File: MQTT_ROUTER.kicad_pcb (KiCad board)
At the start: 2 copper layers, 100 x 100 mm, 84 parts, among them J1 Conn_2Rows-07Pins, J2 Conn_02x07_Odd_Even, J3 Screw_Terminal_01x02, J4 Screw_Terminal_01x03, J5 Screw_Terminal_01x03, J6 Screw_Terminal_01x04, J7 Screw_Terminal_01x06, K1 SANYOU_SRD_Form_C, K2 SANYOU_SRD_Form_C, Q1 SS8050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

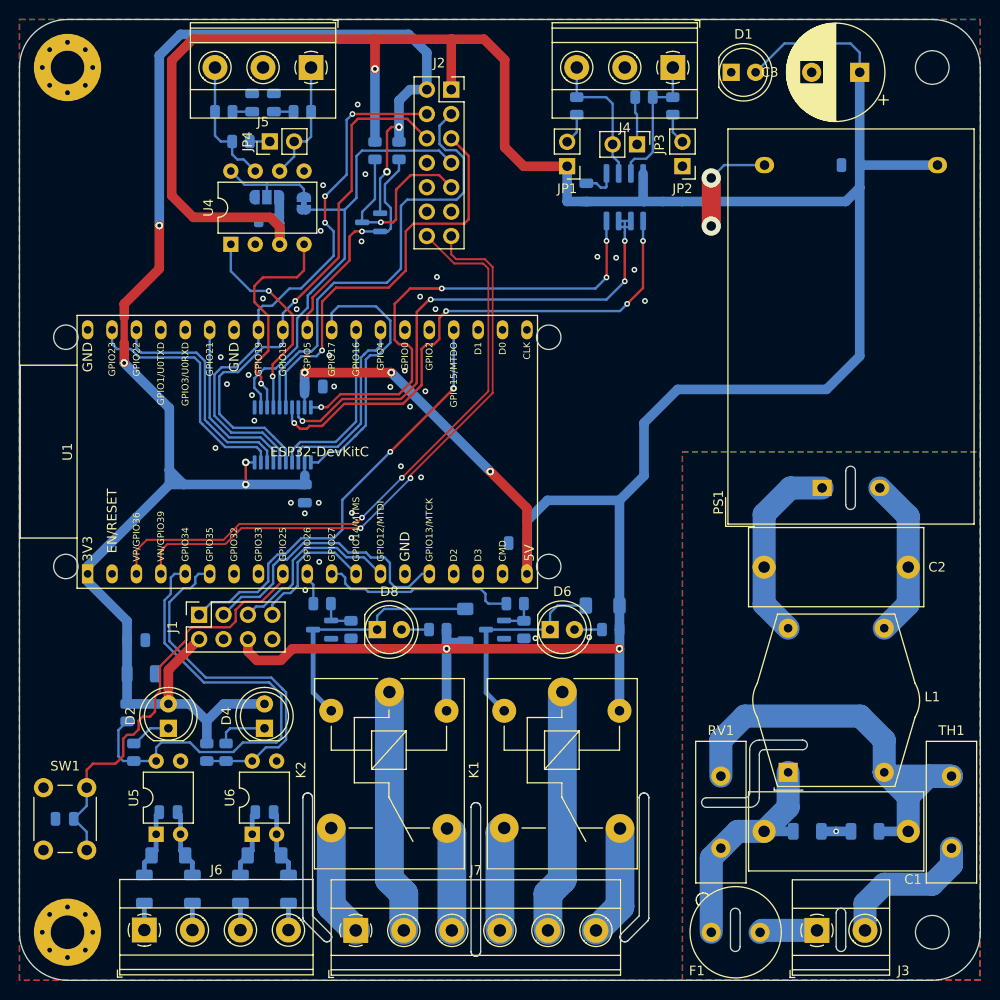
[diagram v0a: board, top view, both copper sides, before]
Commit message: Reparar ubicación de serigrafías y errores de DRC. Mejorar pistas de 5V y 3V.
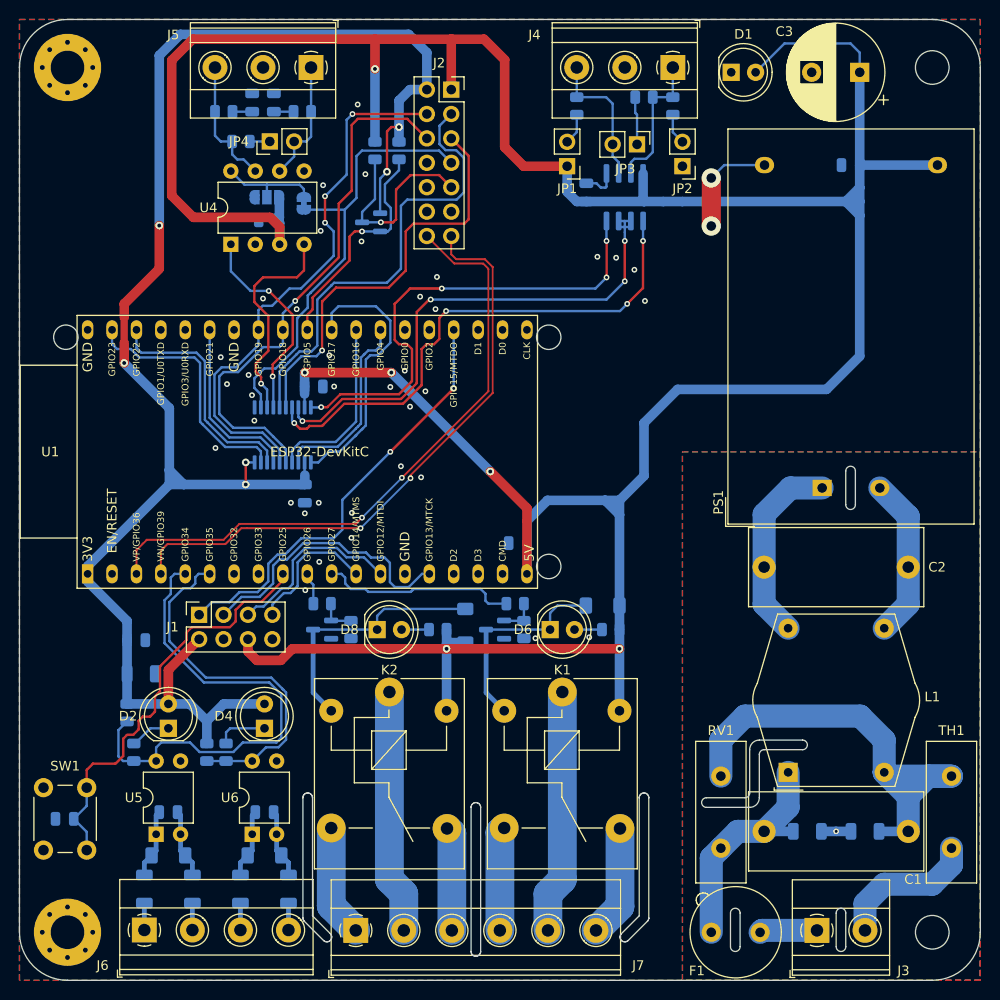
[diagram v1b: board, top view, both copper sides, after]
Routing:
- net +5V: track 347.3 -> 352.4 mm
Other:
- outline, holes or cut-outs redrawn

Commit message: Actualizar componentes, pistas e imágenes
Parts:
- U1: value ESP32-DevKitC -> ESP32-DevKit-USB-C; footprint PCM_Espressif:ESP32-DevKitC -> ESP32:ESP32-DevKit-USB-C
- moved C6 10.2 mm to (140.2, 109.5)
- moved C9 2.52 mm to (125.7, 104.3)
- moved C10 2.50 mm to (126.6, 93.2)
- moved U2 2.50 mm to (123.4, 98.2)
- moved C4 1.50 mm to (183.5, 70.2)
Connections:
- U1 pad 1: +3V3 -> unconnected-(U1-CHIP_PU-Pad1)
- U1 pad 10: /K2 -> /K1
- U1 pad 11: /K1 -> /MTMS
- U1 pad 12: /MTMS -> /MTDI
- U1 pad 13: /MTDI -> /MTCK
- U1 pad 15: /MTCK -> +5V
- U1 pad 16: unconnected-(U1-SD_DATA2/GPIO9-Pad16) -> +3V3
- U1 pad 17: unconnected-(U1-SD_DATA3/GPIO10-Pad17) -> GND
- U1 pad 18: unconnected-(U1-CMD-Pad18) -> /MTDO
- U1 pad 19: +5V -> unconnected-(U1-ADC2_CH2/GPIO2-Pad19)
- U1 pad 2: unconnected-(U1-CHIP_PU-Pad2) -> /S_VP
- U1 pad 20: unconnected-(U1-SD_CLK/GPIO6-Pad20) -> /DERE_LO
- U1 pad 21: unconnected-(U1-SD_DATA0/GPIO7-Pad21) -> /RO_LO
- U1 pad 22: unconnected-(U1-SD_DATA1/GPIO8-Pad22) -> /DI_LO
- U1 pad 23: /MTDO -> /SS_LO
- U1 pad 24: unconnected-(U1-ADC2_CH2/GPIO2-Pad24) -> /SDA_LO
- U1 pad 25: unconnected-(U1-GPIO0/BOOT/ADC2_CH1-Pad25) -> /SCL_LO
- U1 pad 26: /DERE_LO -> /TXD_LO
- U1 pad 27: /RO_LO -> unconnected-(U1-U0RXD/GPIO3-Pad27)
- U1 pad 28: /DI_LO -> unconnected-(U1-U0TXD/GPIO1-Pad28)
- U1 pad 29: /SS_LO -> /RXD_LO
- U1 pad 3: /S_VP -> /S_VN
- U1 pad 30: /SDA_LO -> /RS_LO
- U1 pad 4: /S_VN -> /OP1
- U1 pad 5: /OP1 -> /OP2
- U1 pad 6: /OP2 -> unconnected-(U1-32K_XP/GPIO32/ADC1_CH4-Pad6)
- U1 pad 8: unconnected-(U1-32K_XN/GPIO33/ADC1_CH5-Pad8) -> /CFG_MODE
- U1 pad 9: /CFG_MODE -> /K2
- U2 pad 1: /DI_LO -> /DERE_LO
- U2 pad 17: /RO_HI -> /DI_HI
- U2 pad 18: /DERE_HI -> /RO_HI
- U2 pad 20: /DI_HI -> /DERE_HI
- U2 pad 3: /DERE_LO -> /RO_LO
- U2 pad 4: /RO_LO -> /DI_LO
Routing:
- net +5V: track 352.4 -> 237.9 mm, vias 6 -> 7
- net +3V3: track 175.4 -> 197.2 mm, vias 6 -> 8
- net /DI_LO: track 28.6 -> 19.6 mm
- net /SS_LO: track 24.2 -> 30.0 mm
- net /RS_HI: track 46.4 -> 51.7 mm
- net /DERE_HI: track 55.5 -> 50.6 mm
- net /MTCK: track 29.2 -> 25.0 mm
- net /CFG_MODE: track 43.9 -> 48.0 mm
- net /K1: track 20.5 -> 24.2 mm, vias 0 -> 1
- net /SCL_HI: track 47.6 -> 51.0 mm
- net /MTMS: track 14.4 -> 17.6 mm
- net /SDA_HI: track 43.9 -> 47.0 mm
- net /DERE_LO: track 20.0 -> 16.8 mm
- net /S_VP: track 66.5 -> 63.5 mm
- net /TXD_HI: track 21.7 -> 24.3 mm, vias 2 -> 1
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- added copper zone on B.Cu, net +5V
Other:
- outline, holes or cut-outs redrawn

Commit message: Actualizar PCB
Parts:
- removed F1: 0.5A, Fuse:Fuseholder_TR5_Littelfuse_No560_No460
- removed PS1: HLK-5M05, Converter_ACDC:Converter_ACDC_Hi-Link_HLK-5Mxx
- removed RV1: 14D271K, Capacitor_THT:C_Disc_D14.5mm_W5.0mm_P7.50mm
- added C17: 470uF 16V, Capacitor_THT:CP_Radial_D10.0mm_P5.00mm, F.Cu at (154.2, 79.0)
- added D10: SS36, Diode_SMD:D_SMC, F.Cu at (177.7, 115.2)
- added D11: SS36, Diode_SMD:D_SMC, F.Cu at (168.4, 104.2)
- added D12: 1N47xxA, Diode_THT:D_DO-41_SOD81_P10.16mm_Horizontal, F.Cu at (167.3, 142.4)
- added Q4: IRLZ44N, Package_TO_SOT_THT:TO-220-3_Horizontal_TabDown, F.Cu at (169.5, 139.5)
- added U7: LM2596S-5, Package_TO_SOT_SMD:TO-263-5_TabPin3, F.Cu at (177.7, 101.4)
- C1: value 0.47uF X2 -> 100uF 50V; footprint Capacitor_THT:C_Rect_L18.0mm_W8.0mm_P15.00mm_FKS3_FKP3 -> Capacitor_THT:CP_Radial_D10.0mm_P5.00mm
- C2: value 0.47uF X2 -> 100n; footprint Capacitor_THT:C_Rect_L18.0mm_W8.0mm_P15.00mm_FKS3_FKP3 -> Capacitor_SMD:C_0805_2012Metric; moved to B.Cu
- H1, H2: value MountingHole -> MountingHole_Pad; footprint MountingHole:MountingHole_3.5mm -> MountingHole:MountingHole_3.5mm_Pad_Via
- L1: value L_Coupled -> 47uH; footprint Inductor_THT:Choke_Schaffner_RN112-04-17.7x17.1mm -> Inductor_SMD:L_Bourns_SRR1260
- R1: value 510k -> 100; footprint Resistor_SMD:R_1206_3216Metric -> Resistor_SMD:R_0805_2012Metric
- R2: value 510k -> 20k; footprint Resistor_SMD:R_1206_3216Metric -> Resistor_SMD:R_0805_2012Metric
- TH1: value 8D-10 -> XF250; footprint Capacitor_THT:C_Disc_D14.5mm_W5.0mm_P7.50mm -> Fuse:Fuse_BelFuse_0ZRE0125FF_L21.2mm_W5.3mm
- moved L1 46.1 mm to (176.4, 87.3), turned to 180 degrees
- moved C2 30.6 mm to (172.9, 142.4)
- moved C4 30.4 mm to (170.6, 97.7), turned to -90 degrees
- moved C1 24.1 mm to (167.3, 117.0), turned to 90 degrees
- moved C3 20.3 mm to (171.8, 75.1), turned to 0 degrees
- moved TH1 17.4 mm to (179.4, 134.7)
- moved H1 15.0 mm to (178.5, 150.0)
- moved H2 15.0 mm to (178.5, 60.0)
- moved J3 14.8 mm to (166.7, 149.8)
- moved R2 13.3 mm to (173.6, 136.3)
- moved R3 11.1 mm to (175.7, 67.2), turned to 180 degrees
- moved R1 10.9 mm to (170.1, 136.3)
- moved D1 10.9 mm to (181.2, 67.2), turned to 180 degrees
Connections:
- net /FUENTE/N renamed Net-(J3-Pin_2)
- net Earth renamed Net-(D12-A)
- C1 pad 1: Net-(C1-Pad1) -> /FUENTE/LPROT
- C1 pad 2: Net-(C1-Pad2) -> GND
- C2 pad 1: Net-(PS1-AC/L) -> /FUENTE/LPROT
- C2 pad 2: Net-(PS1-AC/N) -> GND
- J3 pad 1: /FUENTE/L -> GND
- L1 pad 1: Net-(C1-Pad1) -> Net-(D11-K)
- L1 pad 2: Net-(PS1-AC/L) -> +5V
- R1 pad 2: Net-(C1-Pad1) -> Net-(Q4-G)
- R2 pad 2: Net-(C1-Pad2) -> GND
- TH1 pad 2: Net-(C1-Pad2) -> Net-(D10-A)
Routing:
- net Net-(C1-Pad2): track 48.9 -> 0.00 mm
- net /FUENTE/LPROT: track 0.00 -> 47.8 mm
- net Net-(D11-K): track 0.00 -> 37.0 mm
- net +5V: track 237.9 -> 269.2 mm, vias 7 -> 14
- net Net-(C1-Pad1): track 24.6 -> 0.00 mm
- net Net-(PS1-AC/L): track 20.1 -> 0.00 mm
- net Net-(PS1-AC/N): track 16.9 -> 0.00 mm
- net GND: track 14.8 -> 3.70 mm, vias 68 -> 71
- net Net-(D12-A): track 3.07 -> 12.7 mm
- net Net-(D10-A): track 0.00 -> 9.32 mm
- net Net-(J3-Pin_2): track 15.2 -> 21.9 mm
- net /FUENTE/L: track 6.00 -> 0.00 mm
- net Net-(D1-A): track 6.22 -> 2.05 mm
- net Net-(Q4-G): track 0.00 -> 3.31 mm
- removed copper zone on B.Cu, net Net-(D12-A)
- removed copper zone on F.Cu, net Net-(D12-A)
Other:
- board size 100 x 100 mm -> 85 x 100 mm

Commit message: Actualizar zener a 1N4752A (33V)
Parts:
- D12: value 1N47xxA -> 1N4752A
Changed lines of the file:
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@@
 		(tags "LED")
 		(property "Reference" "D1"
-			(at 1.27 -3.96 360)
+			(at 1.27 -3.96 0)
 			(layer "F.SilkS")
 			(effects
@@
 		)
 		(property "Value" "LED_RED"
-			(at 1.27 3.96 360)
+			(at 1.27 3.96 0)
 			(layer "F.Fab")
 			(effects
@@
 		)
 		(property "Footprint" "LED_THT:LED_D5.0mm"
-			(at 0 0 360)
+			(at 0 0 0)
 			(layer "F.Fab")
 			(hide yes)
@@
 		)
 		(property "Datasheet" ""
-			(at 0 0 360)
+			(at 0 0 0)
 			(layer "F.Fab")
 			(hide yes)
@@
 		)
 		(property "Description" "Light emitting diode"
-			(at 0 0 360)
+			(at 0 0 0)
 			(layer "F.Fab")
 			(hide yes)
@@
 		)
 		(fp_text user "${REFERENCE}"
-			(at 1.27 0 360)
+			(at 1.27 0 0)
 			(layer "F.Fab")
 			(effects
@@
 			)
 		)
-		(property "Value" "1N47xxA"
+		(property "Value" "1N4752A"
 			(at 5.08 2.47 0)
 			(layer "F.Fab")
@@
 		(tags "resistor")
 		(property "Reference" "R3"
-			(at 0 1.7 360)
+			(at 0 1.7 0)
 			(layer "B.SilkS")
 			(effects
@@
 		)
 		(property "Value" "330"
-			(at 0 -1.65 360)
+			(at 0 -1.65 0)
 			(layer "B.Fab")
 			(effects
@@
 		)
 		(fp_text user "${REFERENCE}"
-			(at 0 0 360)
+			(at 0 0 0)
 			(layer "B.Fab")
 			(effects

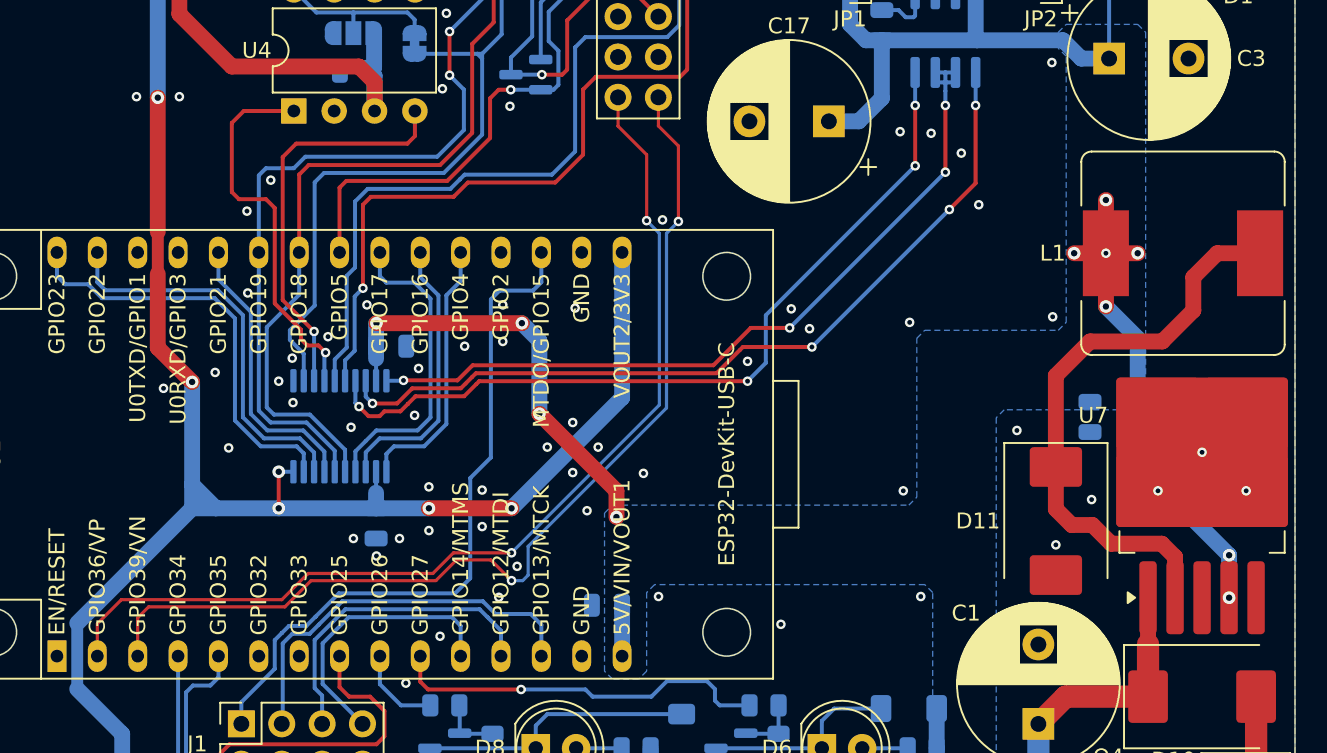
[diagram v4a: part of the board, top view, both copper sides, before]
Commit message: Ajustar grosor de pistas S_VP/S_VN
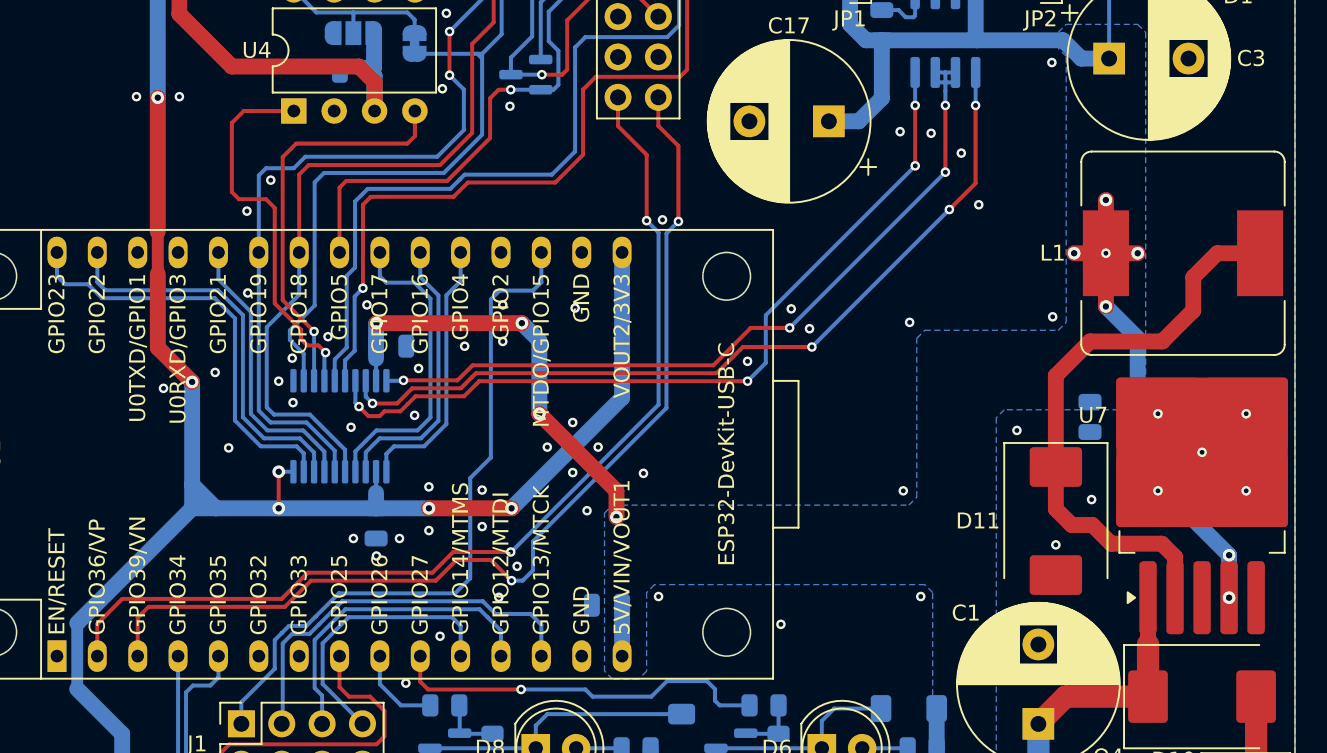
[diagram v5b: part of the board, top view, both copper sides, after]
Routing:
- net GND: vias 71 -> 73
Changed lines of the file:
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@@
+	)
+	(via
+		(at 180.425 97.45)
+		(size 0.6)
+		(drill 0.3)
+		(layers "F.Cu" "B.Cu")
+		(free yes)
+		(net 1)
 	)
 	(via
@@
 	(via
 		(at 151.15 110.7)
+		(size 0.6)
+		(drill 0.3)
+		(layers "F.Cu" "B.Cu")
+		(free yes)
+		(net 1)
+	)
+	(via
+		(at 174.875 97.45)
 		(size 0.6)
 		(drill 0.3)
@@
 	)
 	(segment
+		(start 119.936396 109.6)
+		(end 121.586396 107.95)
+		(width 0.25)
+		(layer "F.Cu")
+		(net 6)
+	)
+	(segment
 		(start 129.436396 107.95)
-		(end 121.586396 107.95)
-		(width 0.2)
-		(layer "F.Cu")
-		(net 6)
-	)
-	(segment
-		(start 119.936396 109.6)
+		(end 130.736396 106.65)
+		(width 0.25)
+		(layer "F.Cu")
+		(net 6)
+	)
+	(segment
+		(start 110.67656 112.7)
+		(end 110.67656 110.28344)
+		(width 0.25)
+		(layer "F.Cu")
+		(net 6)
+	)
+	(segment
+		(start 132.9 106.65)
+		(end 134.2 107.95)
+		(width 0.25)
+		(layer "F.Cu")
+		(net 6)
+	)
+	(segment
+		(start 143.44 79.34)
+		(end 143.44 77.54)
+		(width 0.25)
+		(layer "F.Cu")
+		(net 6)
+	)
+	(segment
+		(start 121.586396 107.95)
+		(end 129.436396 107.95)
+		(width 0.25)
+		(layer "F.Cu")
+		(net 6)
+	)
+	(segment
+		(start 130.736396 106.65)
+		(end 132.9 106.65)
+		(width 0.25)
+		(layer "F.Cu")
+		(net 6)
+	)
+	(segment
+		(start 110.67656 110.28344)
 		(end 111.36 109.6)
-		(width 0.2)
-		(layer "F.Cu")
-		(net 6)
-	)
-	(segment
-		(start 121.586396 107.95)
+		(width 0.25)
+		(layer "F.Cu")
+		(net 6)
+	)
+	(segment
+		(start 144.7 80.6)
+		(end 143.44 79.34)
+		(width 0.25)
+		(layer "F.Cu")
+		(net 6)
+	)
+	(segment
+		(start 111.36 109.6)
 		(end 119.936396 109.6)
-		(width 0.2)
-		(layer "F.Cu")
-		(net 6)
-	)
-	(segment
-		(start 132.9 106.65)
-		(end 130.736396 106.65)
-		(width 0.2)
-		(layer "F.Cu")
-		(net 6)
-	)
-	(segment
-		(start 143.44 77.54)
-		(end 143.44 79.34)
-		(width 0.2)
-		(layer "F.Cu")
-		(net 6)
-	)
-	(segment
-		(start 130.736396 106.65)
-		(end 129.436396 107.95)
-		(width 0.2)
-		(layer "F.Cu")
-		(net 6)
-	)
-	(segment
-		(start 111.36 109.6)
-		(end 110.67656 110.28344)
-		(width 0.2)
-		(layer "F.Cu")
-		(net 6)
-	)
-	(segment
-		(start 134.2 107.95)
-		(end 132.9 106.65)
-		(width 0.2)
-		(layer "F.Cu")
-		(net 6)
-	)
-	(segment
-		(start 144.7 80.6)
-		(end 144.7 85.35)
-		(width 0.2)
-		(layer "F.Cu")
-		(net 6)
-	)
-	(segment
-		(start 110.67656 110.28344)
-		(end 110.67656 112.7)
-		(width 0.2)
-		(layer "F.Cu")
-		(net 6)
-	)
-	(segment
-		(start 143.44 79.34)
+		(width 0.25)
+		(layer "F.Cu")
+		(net 6)
+	)
+	(segment
+		(start 144.7 85.35)
 		(end 144.7 80.6)
-		(width 0.2)
+		(width 0.25)
 		(layer "F.Cu")
 		(net 6)
@@
 	)
 	(segment
-		(start 135.243198 107.606802)
+		(start 135.55 107.3)
 		(end 134.9 107.95)
-		(width 0.2)
+		(width 0.25)
+		(layer "B.Cu")
+		(net 6)
+	)
+	(segment
+		(start 135.55 105.486396)
+		(end 135.55 107.3)
+		(width 0.25)
+		(layer "B.Cu")
+		(net 6)
+	)
+	(segment
+		(start 144.7 85.35)
+		(end 143.95 86.1)
+		(width 0.25)
 		(layer "B.Cu")
 		(net 6)
@@
 	(segment
 		(start 143.95 97.086396)
-		(end 135.243198 105.793198)
-		(width 0.2)
+		(end 135.55 105.486396)
+		(width 0.25)
 		(layer "B.Cu")
 		(net 6)
@@
 		(start 143.95 86.1)
 		(end 143.95 97.086396)
-		(width 0.2)
-		(layer "B.Cu")
-		(net 6)
-	)
-	(segment
-		(start 135.243198 105.793198)
-		(end 135.243198 107.606802)
-		(width 0.2)
+		(width 0.25)
 		(layer "B.Cu")
 		(net 6)
@@
 		(start 134.9 107.95)
 		(end 134.2 107.95)
-		(width 0.2)
-		(layer "B.Cu")
-		(net 6)
-	)
-	(segment
-		(start 144.7 85.35)
-		(end 143.95 86.1)
-		(width 0.2)
+		(width 0.25)
 		(layer "B.Cu")
 		(net 6)
@@
 	)
 	(segment
-		(start 140.9 79.35)
+		(start 142.7 81.15)
+		(end 140.9 79.35)
+		(width 0.25)
+		(layer "F.Cu")
+		(net 8)
+	)
+	(segment
+		(start 142.7 85.3)
 		(end 142.7 81.15)
-		(width 0.2)
-		(layer "F.Cu")
-		(net 8)
-	)
-	(segment
-		(start 142.7 81.15)
-		(end 142.7 85.3)
-		(width 0.2)
-		(layer "F.Cu")
-		(net 8)
-	)
-	(segment
-		(start 129.25 107.5)
-		(end 130.55 106.2)
-		(width 0.2)
-		(layer "F.Cu")
-		(net 8)
-	)
-	(segment
-		(start 130.55 106.2)
-		(end 134.2 106.2)
-		(width 0.2)
-		(layer "F.Cu")
-		(net 8)
-	)
-	(segment
-		(start 109.65 109.15)
-		(end 119.75 109.15)
-		(width 0.2)
-		(layer "F.Cu")
-		(net 8)
-	)
-	(segment
-		(start 140.9 77.54)
-		(end 140.9 79.35)
-		(width 0.2)
+		(width 0.25)
+		(layer "F.Cu")
+		(net 8)
+	)
+	(segment
+		(start 130.236396 106.442893)
+		(end 130.529289 106.15)
+		(width 0.25)
+		(layer "F.Cu")
+		(net 8)
+	)
+	(segment
+		(start 121.086396 107.742893)
+		(end 121.379289 107.45)
+		(width 0.25)
+		(layer "F.Cu")
+		(net 8)
+	)
+	(segment
+		(start 121.379289 107.45)
+		(end 129.22929 107.45)
+		(width 0.25)
+		(layer "F.Cu")
+		(net 8)
+	)
+	(segment
+		(start 130.529289 106.15)
+		(end 134.15 106.15)
+		(width 0.25)
+		(layer "F.Cu")
+		(net 8)
+	)
+	(segment
+		(start 109.7 109.1)
+		(end 119.72929 109.1)
+		(width 0.25)
+		(layer "F.Cu")
+		(net 8)
+	)
+	(segment
+		(start 120.739645 108.089645)
+		(end 121.086396 107.742893)
+		(width 0.25)
+		(layer "F.Cu")
+		(net 8)
+	)
+	(segment
+		(start 119.72929 109.1)
+		(end 120.739645 108.089645)
+		(width 0.25)
+		(layer "F.Cu")
+		(net 8)
+	)
+	(segment
+		(start 129.22929 107.45)
+		(end 129.839645 106.839645)
+		(width 0.25)
 		(layer "F.Cu")
 		(net 8)
@@
 	(segment
 		(start 108.13656 110.66344)
-		(end 109.65 109.15)
-		(width 0.2)
-		(layer "F.Cu")
-		(net 8)
-	)
-	(segment
-		(start 119.75 109.15)
-		(end 121.4 107.5)
-		(width 0.2)
+		(end 109.7 109.1)
+		(width 0.25)
 		(layer "F.Cu")
 		(net 8)
@@
 		(start 108.13656 112.7)
 		(end 108.13656 110.66344)
-		(width 0.2)
-		(layer "F.Cu")
-		(net 8)
-	)
-	(segment
-		(start 121.4 107.5)
-		(end 129.25 107.5)
-		(width 0.2)
-		(layer "F.Cu")
-		(net 8)
-	)
-	(via
-		(at 134.2 106.2)
+		(width 0.25)
+		(layer "F.Cu")
+		(net 8)
+	)
+	(segment
+		(start 129.839645 106.839645)
+		(end 130.236396 106.442893)
+		(width 0.25)
+		(layer "F.Cu")
+		(net 8)
+	)
+	(segment
+		(start 140.9 79.35)
+		(end 140.9 77.54)
+		(width 0.25)
+		(layer "F.Cu")
+		(net 8)
+	)
+	(via
+		(at 134.15 106.15)
 		(size 0.6)
 		(drill 0.3)
@@
 	)
 	(segment
-		(start 143.5 86.1)
-		(end 142.7 85.3)
-		(width 0.2)
-		(layer "B.Cu")
-		(net 8)
-	)
-	(segment
-		(start 143.5 96.9)
-		(end 143.5 86.1)
-		(width 0.2)
-		(layer "B.Cu")
-		(net 8)
-	)
-	(segment
-		(start 134.2 106.2)
-		(end 143.5 96.9)
-		(width 0.2)
-		(layer "B.Cu")
-		(net 8)
+		(start 134.17929 106.15)
+		(end 134.15 106.15)
+		(width 0.25)
+		(layer "B.Cu")
+		(net 8)
+	)
+	(segment
+		(start 143.45 96.87929)
+		(end 134.17929 106.15)
+		(width 0.25)
+		(layer "B.Cu")
+		(net 8)
+	)
+	(segment
+		(start 142.7 85.3)
+		(end 143.45 86.05)
+		(width 0.25)
+		(layer "B.Cu")
+		(net 8)
+	)
+	(segment
+		(start 143.45 86.05)
+		(end 143.45 96.87929)
+		(width 0.25)
+		(layer "B.Cu")
+		(net 8)
